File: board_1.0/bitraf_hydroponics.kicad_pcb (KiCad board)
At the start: 2 copper layers, 67.3 x 86.4 mm, 36 parts, among them P1 12V_PWR, P10 ROT_BTN, P11 BUZZ, P12 LDR, P13 MOS_OUT_2, P14 MOS_OUT_1, P15 MOS_OUT_3, P17 BREAKOUT_1-15, P18 BREAKOUT_16-30, P2 I2C_1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

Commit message: o Removing old PCB layout.
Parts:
- removed C1, C4: CP, Capacitors_THT:CP_Radial_D5.0mm_P2.50mm
- removed C2, C3: C, Capacitors_THT:C_Disc_D3.0mm_W2.0mm_P2.50mm
- removed D1, D2, D3: D, Diodes_THT:D_DO-41_SOD81_P10.16mm_Horizontal
- removed P1: 12V_PWR, Terminal_Blocks:TerminalBlock_Pheonix_MKDS1.5-2pol
- removed P10: ROT_BTN, Pin_Headers:Pin_Header_Straight_1x05_Pitch2.54mm
- removed P11: BUZZ, Pin_Headers:Pin_Header_Straight_1x02_Pitch2.54mm
- removed P12: LDR, Pin_Headers:Pin_Header_Straight_1x02_Pitch2.54mm
- removed P13: MOS_OUT_2, Terminal_Blocks:TerminalBlock_Pheonix_MKDS1.5-2pol
- removed P14: MOS_OUT_1, Terminal_Blocks:TerminalBlock_Pheonix_MKDS1.5-2pol
- removed P15: MOS_OUT_3, Terminal_Blocks:TerminalBlock_Pheonix_MKDS1.5-2pol
- removed P17: BREAKOUT_1-15, Pin_Headers:Pin_Header_Straight_1x15_Pitch2.54mm
- removed P18: BREAKOUT_16-30, Pin_Headers:Pin_Header_Straight_1x15_Pitch2.54mm
- removed P2: I2C_1, Pin_Headers:Pin_Header_Straight_1x04_Pitch2.54mm
- removed P3: I2C_2, Pin_Headers:Pin_Header_Straight_1x04_Pitch2.54mm
- removed P4: I2C_3, Pin_Headers:Pin_Header_Straight_1x04_Pitch2.54mm
- removed P5: TEMP_HUM, Pin_Headers:Pin_Header_Straight_1x03_Pitch2.54mm
- removed P7: I2C_4, Pin_Headers:Pin_Header_Straight_1x04_Pitch2.54mm
- removed P8: Radio_433, Pin_Headers:Pin_Header_Straight_1x03_Pitch2.54mm
- removed P9: LCD, Pin_Headers:Pin_Header_Straight_1x04_Pitch2.54mm
- removed Q1, Q2, Q3: Q_NMOS_GDS, TO_SOT_Packages_THT:TO-220_Vertical
- removed R2: R, Resistors_THT:R_Axial_DIN0207_L6.3mm_D2.5mm_P10.16mm_Horizontal
- removed R3, R4, R5: 10k, Resistors_THT:R_Axial_DIN0207_L6.3mm_D2.5mm_P10.16mm_Horizontal
- removed REF** (x4): MountingHole_3mm, Mounting_Holes:MountingHole_3mm
- removed U1: NodeMCU_1.0, NodeMCU:NodeMCU
- removed U2: 5v_LDO, TO_SOT_Packages_THT:TO-220_Vertical
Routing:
- net GND: track 399.1 -> 0.00 mm, vias 2 -> 0
- net +3V3: track 139.2 -> 0.00 mm
- net +5V: track 135.6 -> 0.00 mm
- net +12V: track 127.0 -> 0.00 mm
- net /LDR_PIN: track 89.7 -> 0.00 mm
- net /BUZZ: track 75.2 -> 0.00 mm
- net /SCL: track 72.8 -> 0.00 mm
- net /SDA: track 70.9 -> 0.00 mm
- net /ROT_SW: track 62.6 -> 0.00 mm
- net /TEMP_HUM: track 56.7 -> 0.00 mm
- net /ROT_1: track 56.7 -> 0.00 mm
- net /ROT_0: track 50.1 -> 0.00 mm
- net /MOS_1: track 40.2 -> 0.00 mm
- net /RF_DATA: track 30.1 -> 0.00 mm
- net /MOS_2: track 29.7 -> 0.00 mm
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- removed copper zone on B.Cu, net GND
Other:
- board outline removed
- board text removed: "12V"
- board text removed: "3v"
- board text removed: "5v"
- board text removed: "Bitraf - Hydroponics v0.0.2"
- board text removed: "GND"
- board text removed: "LDR"
- board text removed: "Rotary"
- board text removed: "SCL"
- board text removed: "SDA"
- board text removed: "TEMP"

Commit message: o Selecting the rest of the footprints. Using 0805 as default SMD size to make it makerspace friendly. o Some more nitpicking.
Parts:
- added C1: 0.1u, Capacitors_SMD:C_0805, F.Cu at (176.9, 58.6)
- added C2: 10u, Capacitors_SMD:C_0805, F.Cu at (182.0, 66.9)
- added C3: 0.1u, Capacitors_SMD:C_0805, F.Cu at (173.4, 43.8)
- added C4: 75p, Capacitors_SMD:C_0805, F.Cu at (148.4, 88.1)
- added C5: 22u, Capacitors_SMD:C_0805, F.Cu at (191.0, 38.8)
- added C6: 22u, Capacitors_SMD:C_0805, F.Cu at (113.5, 90.0)
- added C7: 4.7µ, Capacitors_SMD:C_0805, F.Cu at (150.5, 44.0)
- added C8: 4.7µ, Capacitors_SMD:C_0805, F.Cu at (144.0, 65.0)
- added D1, D2, D3: S1MTR, Diodes_SMD:D_SMA_Handsoldering, F.Cu at (148.5, 105.0)
- added L1: 15u, Inductors_SMD:L_Taiyo-Yuden_NR-80xx, F.Cu at (220.7, 55.0)
- added P1: 12V_PWR, Connectors_Terminal_Blocks:TerminalBlock_Pheonix_PT-3.5mm_2pol, F.Cu at (206.5, 109.2)
- added P10: I2C_4, Pin_Headers:Pin_Header_Straight_1x04_Pitch2.54mm, F.Cu at (121.8, 64.7)
- added P11: BUZZ, Connectors_Phoenix:PhoenixContact_PTSM0,5_4-HV-2,5_SMD, F.Cu at (144.0, 54.2)
- added P12: LDR, Connectors_Phoenix:PhoenixContact_PTSM0,5_4-HV-2,5_SMD, F.Cu at (165.3, 105.6)
- added P13: TEMP_HUM, Pin_Headers:Pin_Header_Straight_1x03_Pitch2.54mm, F.Cu at (189.5, 100.1)
- added P14: PROGRAMMER, Pin_Headers:Pin_Header_Straight_1x06_Pitch2.54mm, F.Cu at (110.5, 98.7)
- added P15: LCD, Pin_Headers:Pin_Header_Straight_1x06_Pitch2.54mm, F.Cu at (181.8, 105.7)
- added P16: Radio_433, Socket_Strips:Socket_Strip_Straight_1x03_Pitch2.54mm, F.Cu at (184.2, 77.2)
- added P2: SWITCH_1, Connectors_Phoenix:PhoenixContact_PTSM0,5_4-HV-2,5_SMD, F.Cu at (193.1, 60.1)
- added P3: SWITCH_2, Connectors_Phoenix:PhoenixContact_PTSM0,5_4-HV-2,5_SMD, F.Cu at (151.3, 126.6)
- added P4: SWITCH_3, Connectors_Phoenix:PhoenixContact_PTSM0,5_4-HV-2,5_SMD, F.Cu at (157.8, 55.5)
- added P5: LCD, Pin_Headers:Pin_Header_Straight_1x04_Pitch2.54mm, F.Cu at (196.4, 79.1)
- added P6: ROT_ENC, Pin_Headers:Pin_Header_Straight_1x05_Pitch2.54mm, F.Cu at (129.3, 97.6)
- added P7: I2C_1, Pin_Headers:Pin_Header_Straight_1x04_Pitch2.54mm, F.Cu at (133.8, 120.6)
- added P8: I2C_2, Pin_Headers:Pin_Header_Straight_1x04_Pitch2.54mm, F.Cu at (164.7, 118.4)
- added P9: I2C_3, Pin_Headers:Pin_Header_Straight_1x04_Pitch2.54mm, F.Cu at (137.1, 80.5)
- added Q1, Q2, Q3: DMN2041L-7, TO_SOT_Packages_SMD:SOT-23, F.Cu at (148.5, 105.0)
- added R1: 10k, Resistors_SMD:R_0805, F.Cu at (138.0, 46.4)
- added R2: 10k, Resistors_SMD:R_0805, F.Cu at (135.6, 75.5)
- added R3: 10k, Resistors_SMD:R_0805, F.Cu at (127.9, 83.4)
- added R4: 100k, Resistors_SMD:R_0805, F.Cu at (102.7, 74.4)
- added R5: 13.3k, Resistors_SMD:R_0805, F.Cu at (168.8, 62.3)
- added R6: R, Resistors_SMD:R_0805, F.Cu at (136.7, 63.2)
- added U1: TPS54202, TO_SOT_Packages_SMD:SOT-23-6_Handsoldering, F.Cu at (148.5, 105.0)
- added U2: AP2114H-3.3TRG1, TO_SOT_Packages_SMD:SOT-223, F.Cu at (148.5, 105.0)
- added U3: ESP-12F, ESP8266:ESP-12E, F.Cu at (157.9, 79.7)
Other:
- board outline added: 50 x 50 mm

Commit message: rough sort of components
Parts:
- moved P13 128.6 mm to (64.8, 68.6)
- moved P16 119.4 mm to (64.8, 81.3)
- moved P15 113.7 mm to (68.6, 95.2)
- moved P5 104.4 mm to (94.0, 99.1)
- moved P8 98.3 mm to (80.0, 68.6)
- moved P12 86.1 mm to (101.1, 48.3)
- moved C7 81.8 mm to (121.9, 120.7), turned to 90 degrees
- moved P3 78.6 mm to (158.0, 48.3)
- moved P7 77.6 mm to (76.2, 68.6)
- moved Q3 70.4 mm to (174.0, 39.4)
- moved R3 67.3 mm to (174.0, 34.3)
- moved C5 67.0 mm to (171.4, 102.9)
- moved Q2 66.1 mm to (158.5, 39.7)
- moved Q1 65.8 mm to (143.5, 39.4)
- moved L1 63.0 mm to (170.2, 92.7), turned to 180 degrees
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
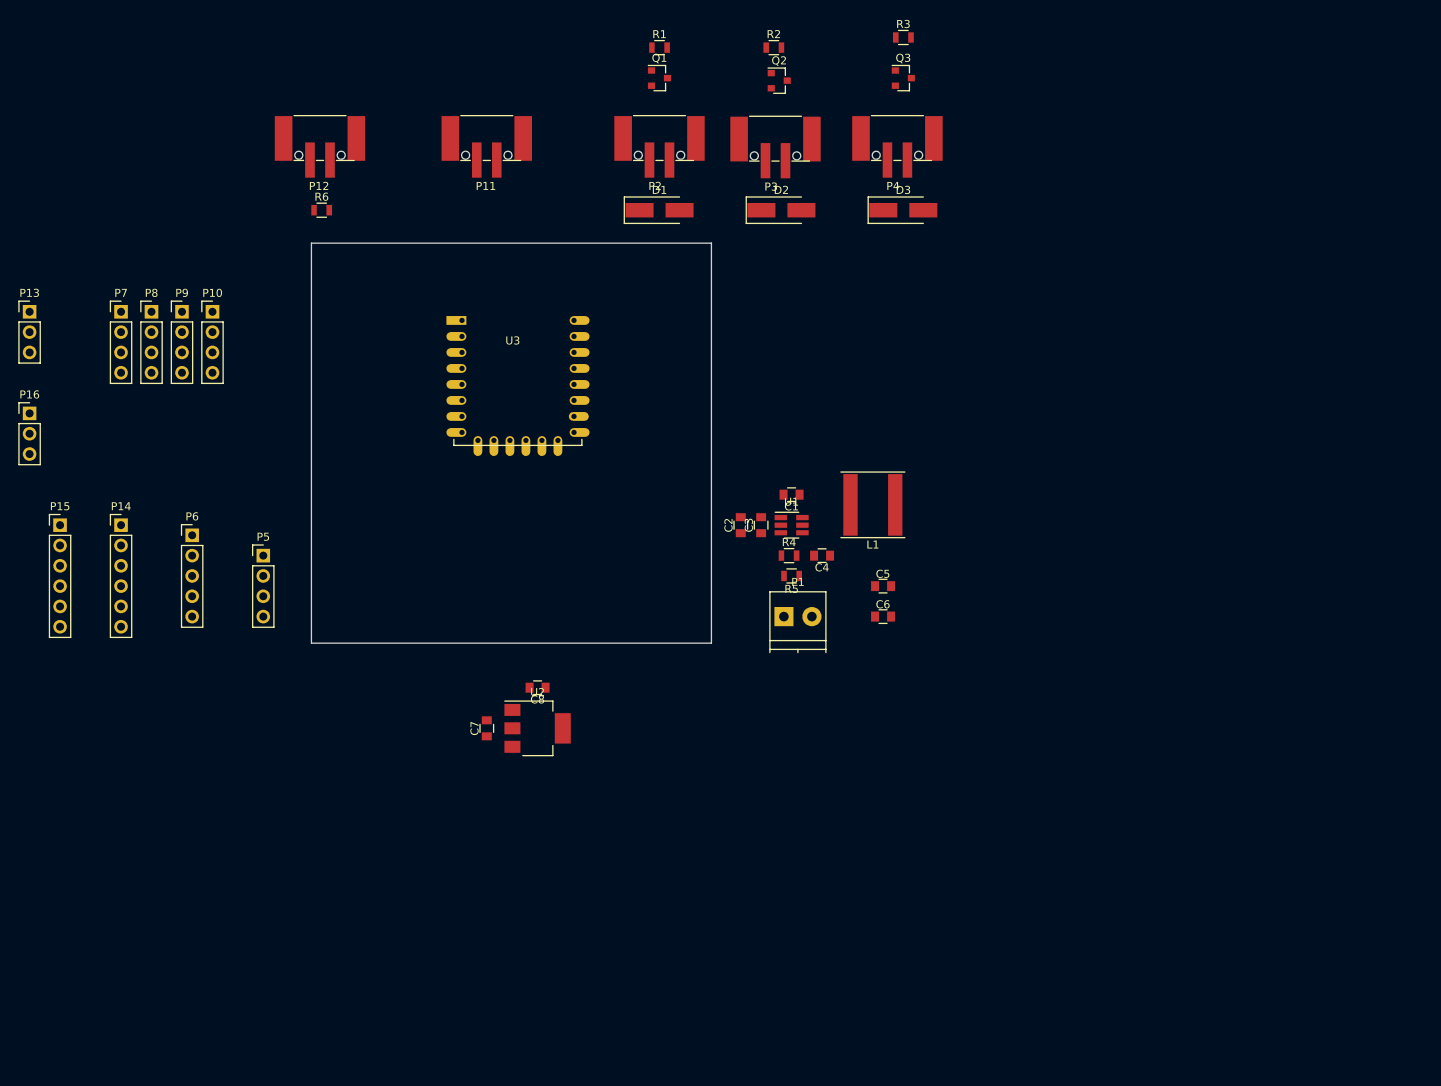
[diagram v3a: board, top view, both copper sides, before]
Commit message: schematic: o Changing 12V connector to the same as the rest. o Better label for Radio. o Changing R6 from SMD to THT so it is easier to customize with the LDR. pcb: o Adding copper zones connected to GND on front and back. o Expanding board to 50x100 mm. Moving all connectors onto board.
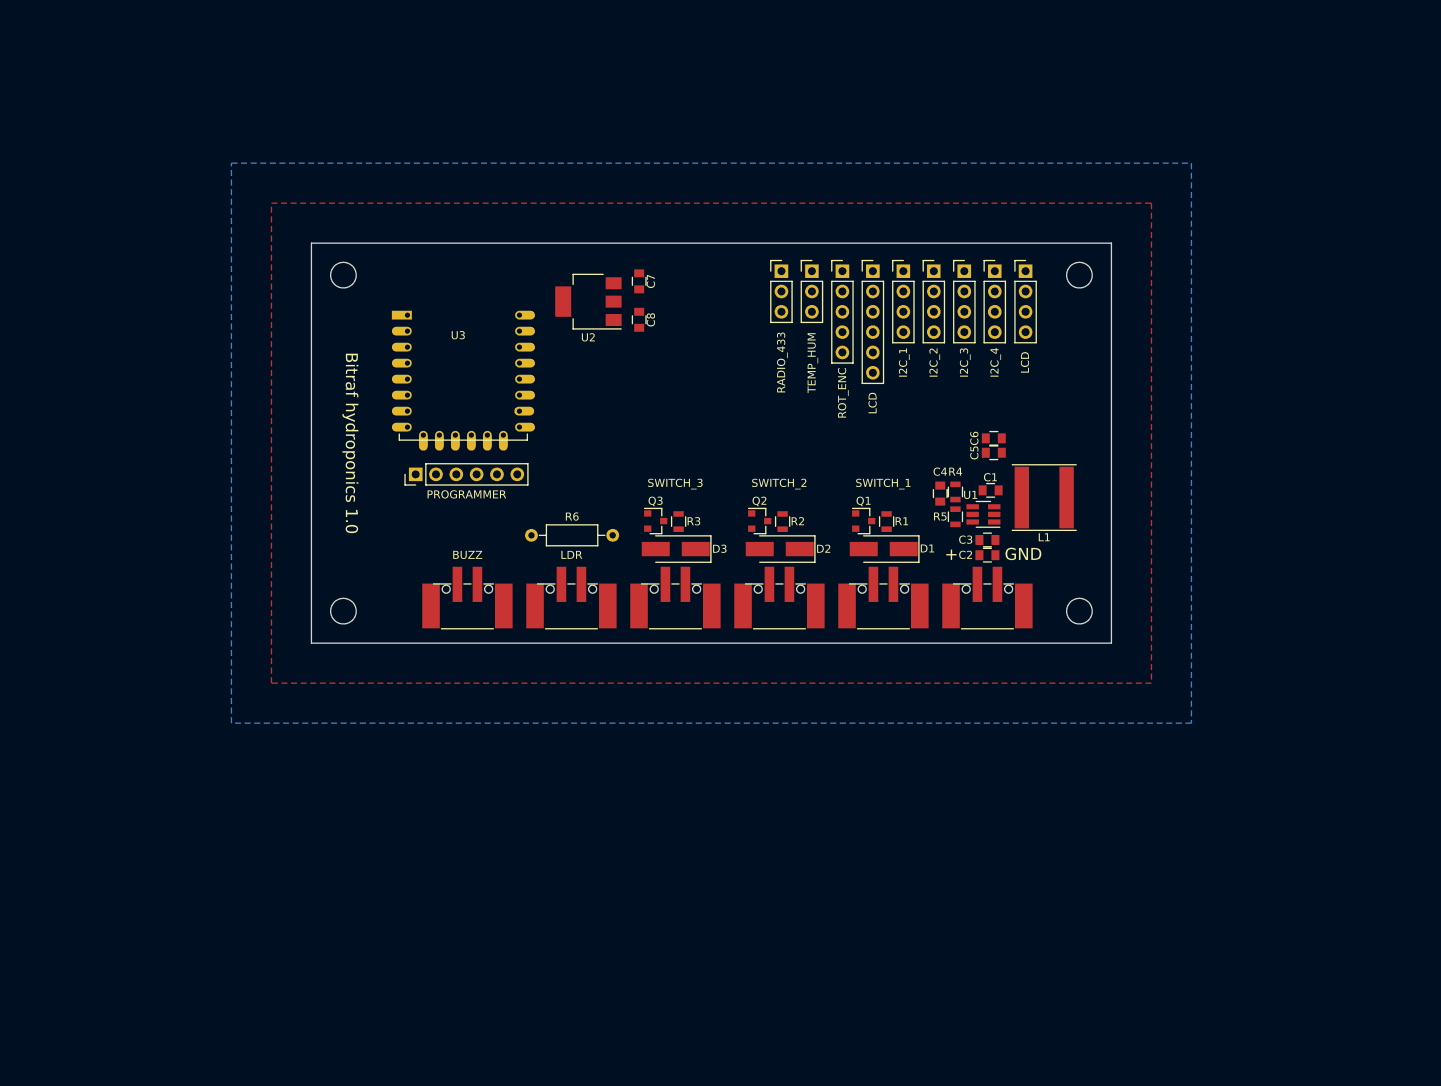
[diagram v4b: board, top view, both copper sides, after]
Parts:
- added REF**: MountingHole_3.2mm_M3, Mounting_Holes:MountingHole_3.2mm_M3, F.Cu at (104.0, 64.0)
- added REF**: MountingHole_3.2mm_M3, Mounting_Holes:MountingHole_3.2mm_M3, F.Cu at (196.0, 64.0)
- added REF**: MountingHole_3.2mm_M3, Mounting_Holes:MountingHole_3.2mm_M3, F.Cu at (196.0, 106.0)
- added REF**: MountingHole_3.2mm_M3, Mounting_Holes:MountingHole_3.2mm_M3, F.Cu at (104.0, 106.0)
- P1: value 12V_PWR -> 12V; footprint Connectors_Terminal_Blocks:TerminalBlock_Pheonix_PT-3.5mm_2pol -> Connectors_Phoenix:PhoenixContact_PTSM0,5_4-HV-2,5_SMD
- P16: value Radio_433 -> RADIO_433
- R6: footprint Resistors_SMD:R_0805 -> Resistors_THT:R_Axial_DIN0207_L6.3mm_D2.5mm_P10.16mm_Horizontal
- moved P15 106.4 mm to (170.2, 63.5)
- moved P5 101.7 mm to (189.3, 63.5)
- moved P9 97.9 mm to (181.6, 63.5)
- moved P13 97.9 mm to (162.6, 63.5)
- moved P7 97.9 mm to (174.0, 63.5)
- moved P8 97.9 mm to (177.8, 63.5)
- moved P10 97.9 mm to (185.4, 63.5)
- moved P16 95.6 mm to (158.8, 63.5)
- moved P6 87.7 mm to (166.4, 63.5)
- moved R3 66.7 mm to (145.9, 94.8), turned to 270 degrees
- moved R1 65.7 mm to (171.9, 94.8), turned to 270 degrees
- moved P12 64.0 mm to (132.5, 104.0), turned to 180 degrees
- moved Q3 63.4 mm to (143.0, 94.7)
- moved P2 62.4 mm to (171.5, 104.0), turned to 180 degrees
- moved P4 62.3 mm to (145.5, 104.0), turned to 180 degrees
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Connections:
- R4 pad 1: Net-(R4-Pad1) -> +5V
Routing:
- added copper zone on B.Cu, net GND
- added copper zone on F.Cu, net GND
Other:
- board size 50 x 50 mm -> 100 x 50 mm
- board text added: "+"
- board text added: "Bitraf hydroponics 1.0"
- board text added: "GND"

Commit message: everything connected. Ugly and thin tracks where they should be wider, but passes test.
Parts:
- P15: value LCD -> SPI
- moved D3 26.0 mm to (171.6, 98.2)
- moved Q3 26.0 mm to (169.1, 94.7)
- moved D1 26.0 mm to (145.5, 98.2)
- moved P2 26.0 mm to (145.5, 104.0)
- moved P4 26.0 mm to (171.5, 104.0)
- moved Q1 26.0 mm to (143.0, 94.7)
- moved R1 26.0 mm to (145.9, 94.8)
- moved R3 26.0 mm to (171.9, 94.8)
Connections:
- P10 pad 2: /SDA -> /SCL
- P10 pad 3: /SCL -> /SDA
- P7 pad 2: /SDA -> /SCL
- P7 pad 3: /SCL -> /SDA
- P8 pad 2: /SDA -> /SCL
- P8 pad 3: /SCL -> /SDA
- P9 pad 2: /SDA -> /SCL
- P9 pad 3: /SCL -> /SDA
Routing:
- net GND: track 0.00 -> 291.5 mm, vias 0 -> 5
- net +12V: track 0.00 -> 124.6 mm, vias 0 -> 4
- net +5V: track 0.00 -> 102.1 mm
- net +3V3: track 0.00 -> 93.5 mm, vias 0 -> 4
- net /SCL: track 0.00 -> 85.4 mm
- net /SDA: track 0.00 -> 82.5 mm
- net /SWITCH_3: track 0.00 -> 81.8 mm
- net /SPI_MOSI: track 0.00 -> 74.5 mm, vias 0 -> 1
- net /SWITCH_2: track 0.00 -> 71.7 mm
- net /SPI_CS: track 0.00 -> 71.1 mm, vias 0 -> 2
- net /SPI_MISO: track 0.00 -> 60.3 mm, vias 0 -> 2
- net /SPI_SCL: track 0.00 -> 60.1 mm, vias 0 -> 2
- net /SWITCH_1: track 0.00 -> 59.9 mm
- net /TEMP_HUM: track 0.00 -> 51.9 mm, vias 0 -> 1
- net /ROT_SW: track 0.00 -> 47.5 mm
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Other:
- net class Default: clearance 0.254 -> 0.15; trace_width 0.508 -> 0.15
- rule trace_clearance: 0.254 -> 0.15

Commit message: Hmm. found a few unconnected Gnd's not picked up by test
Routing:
- net GND: track 291.5 -> 311.7 mm, vias 5 -> 8
- net /SWITCH_2: track 71.7 -> 68.4 mm
- net /SWITCH_3: track 81.8 -> 78.9 mm
- net /SWITCH_1: track 59.9 -> 57.2 mm
- net /BUZZ: track 36.3 -> 35.1 mm
- net /SPI_CS: track 71.1 -> 72.1 mm

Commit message: cleanup
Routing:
- net +3V3: track 93.4 -> 103.1 mm
- net /SPI_MOSI: track 74.5 -> 78.4 mm
- net GND: track 311.7 -> 314.2 mm
- net /LDR: track 45.8 -> 47.3 mm
- net /CH_PD: track 19.4 -> 20.8 mm
- net +5V: track 102.1 -> 101.0 mm
- net /RF_DATA: track 47.3 -> 48.3 mm
- net /ROT_0: track 42.8 -> 43.8 mm
- net +12V: track 124.6 -> 123.7 mm
- net /SPI_MISO: track 60.3 -> 60.9 mm
